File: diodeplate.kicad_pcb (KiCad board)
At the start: 2 copper layers, 164 x 164 mm, 85 parts, among them SW1 TS-1185EC-C-D-B, SW2 TS-1185EC-C-D-B, SW3 TS-1185EC-C-D-B, U1 ESP32-WROOM-32E, U2 CP2102-GMR, U3 U262-161N-4BVC11, U4 BL1117-33CX, U5 UMH3N, U6 SN74AHCT32QPWRQ1

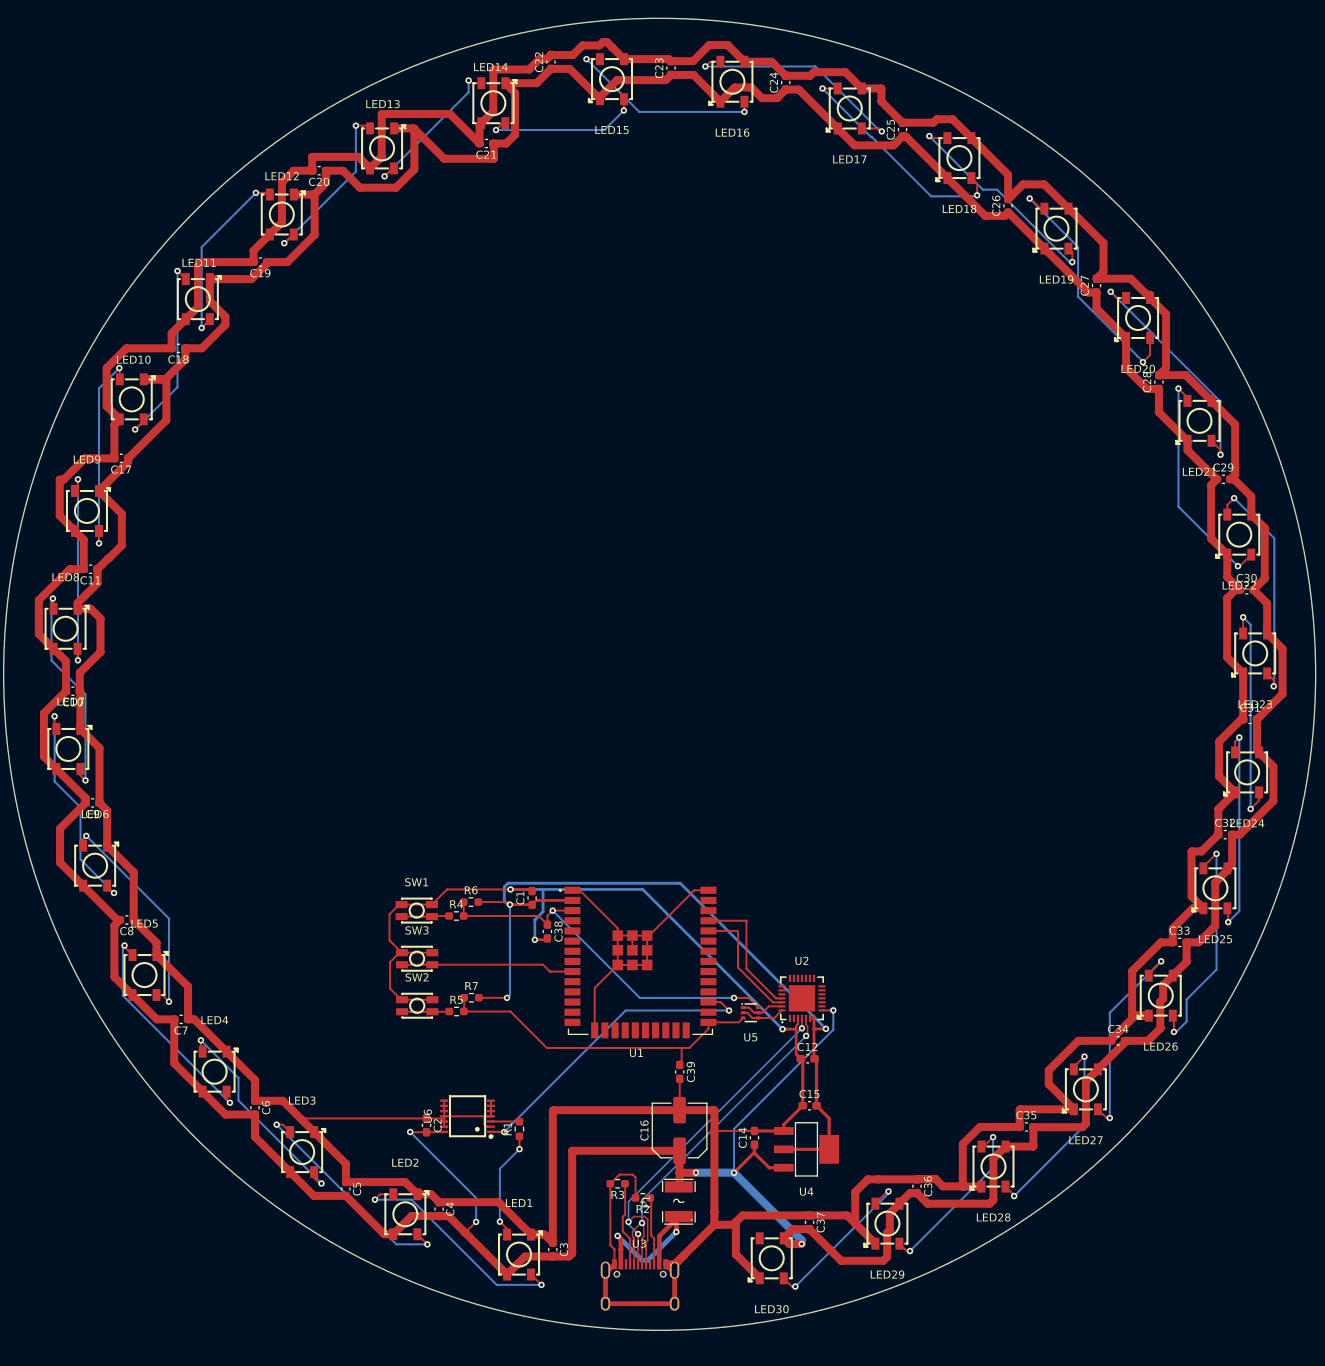
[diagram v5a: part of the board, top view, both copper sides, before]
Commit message: add open hardware logo and some text, resolved warnings
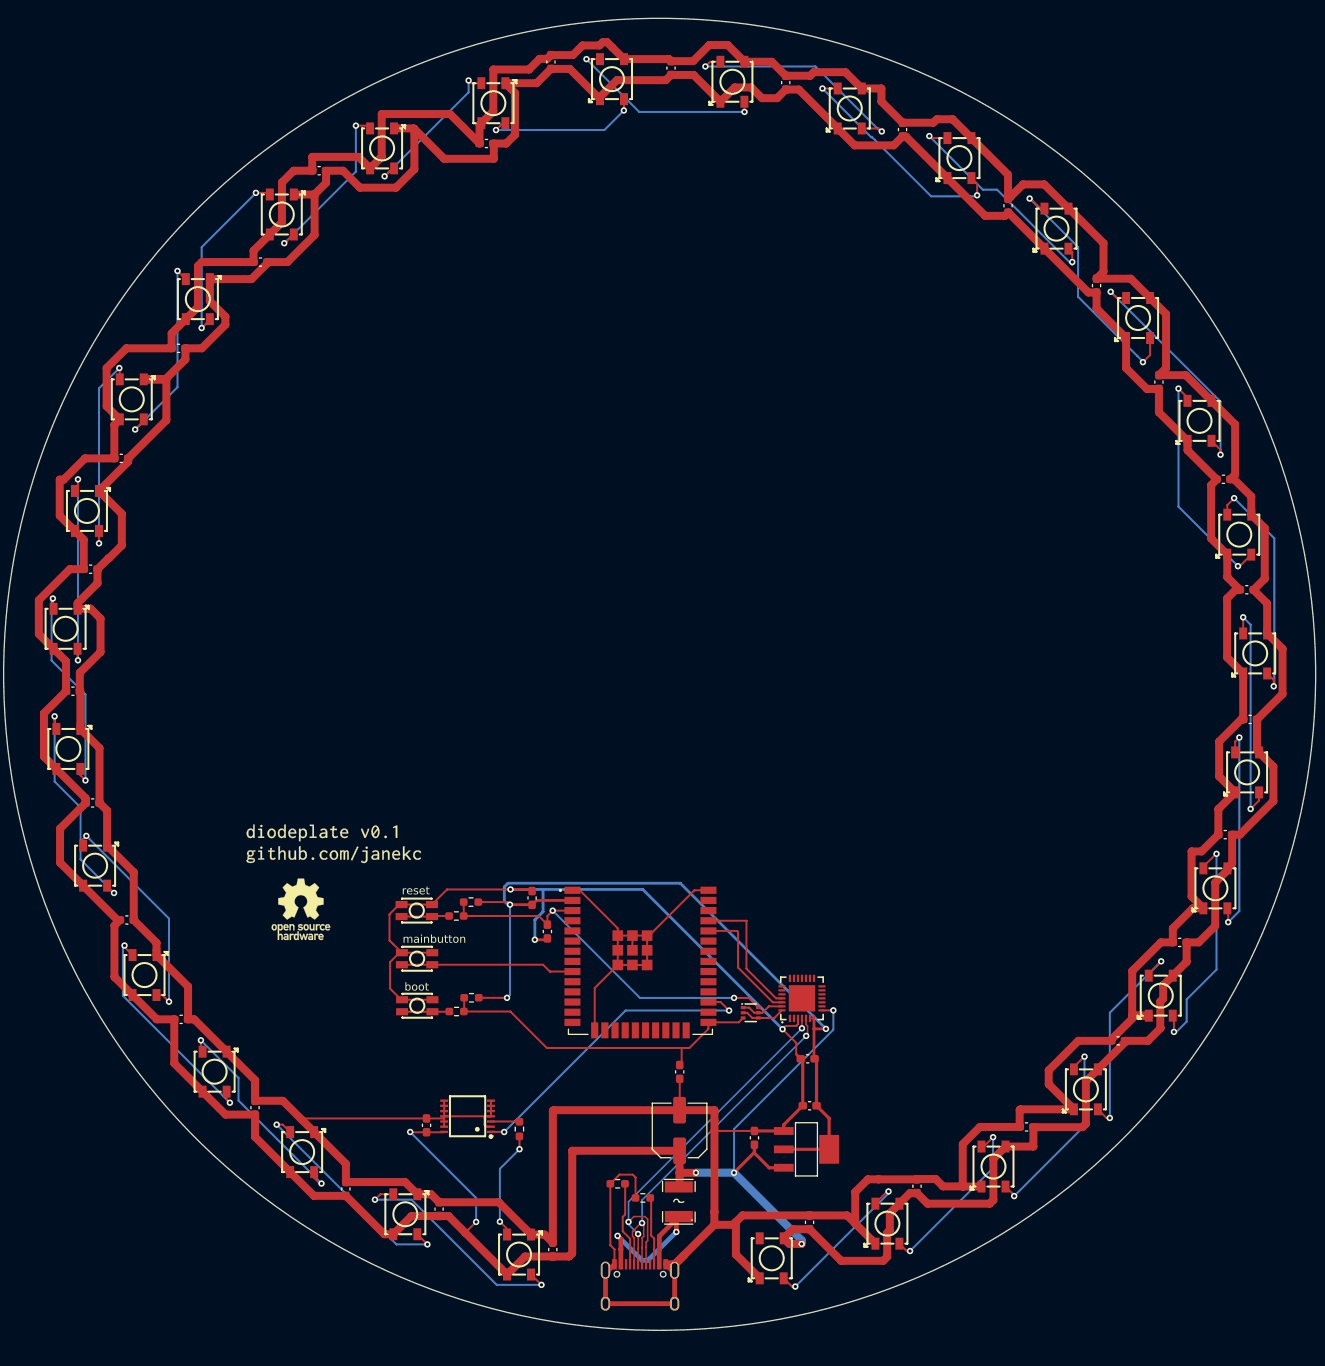
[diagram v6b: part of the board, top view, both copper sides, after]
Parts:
- renumbered SW2 to boot, SW3 to mainbutton, SW1 to reset
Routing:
- net +5V: track 665.0 -> 664.1 mm
